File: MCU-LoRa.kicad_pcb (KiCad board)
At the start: 2 copper layers, 22.9 x 49 mm, 40 parts, among them J7 castellated_1x08_P2.54, J8 castellated_1x08_P2.54, J9 Conn_02x04_Top_Bottom, SW1 SW_Push, SW2 SW_Push, U1 RFM95W-915S2, U2 STM32F411CEU6, Y1 32.758kHz, Y2 25MHz

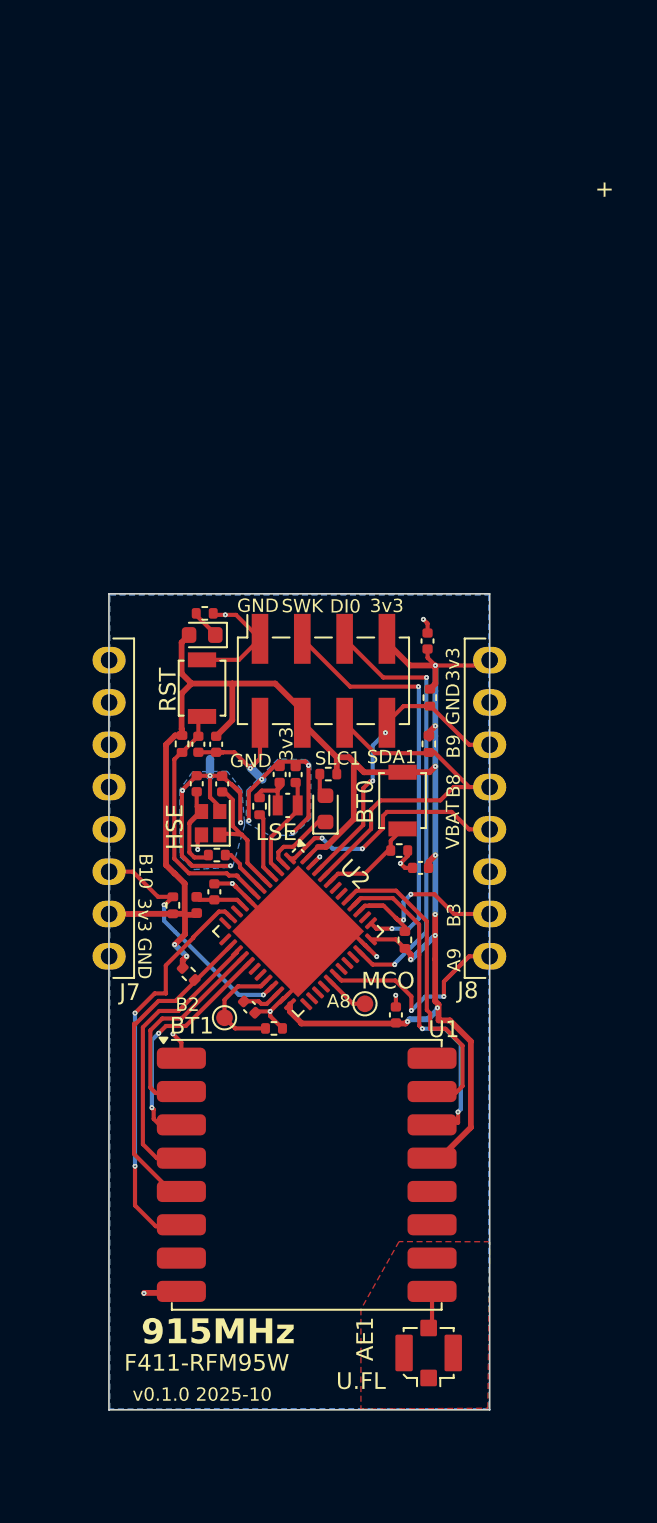
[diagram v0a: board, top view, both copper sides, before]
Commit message: reduced with of board.
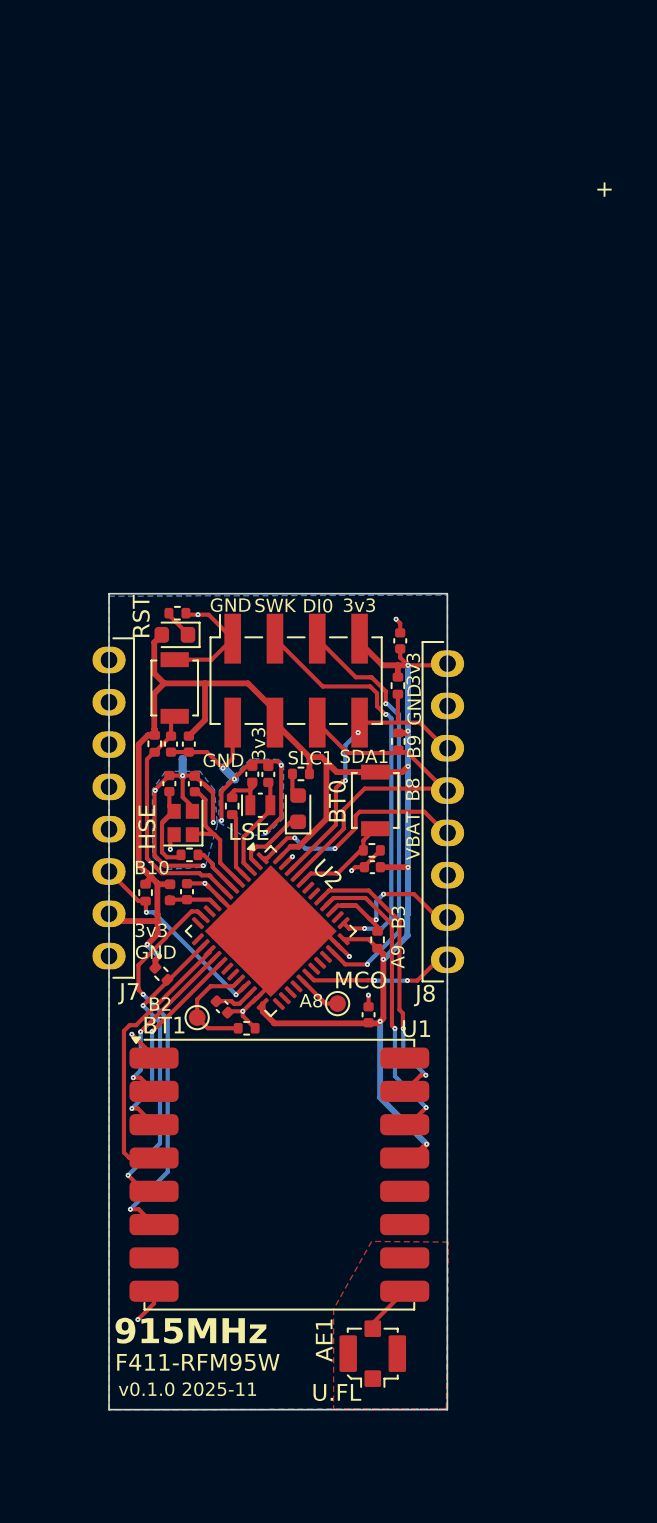
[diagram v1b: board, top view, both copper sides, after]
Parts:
- U2: footprint Package_DFN_QFN:QFN-48-1EP_7x7mm_P0.5mm_EP5.6x5.6mm -> ProjectLib:QFN-48-1EP_7x7mm_P0.5mm_EP5.6x5.6mm
- moved AE1 3.36 mm to (65.4, 91.9)
- moved C4 2.89 mm to (65.4, 62.7)
- moved J8 2.54 mm to (69.9, 59.3)
- moved R10 2.05 mm to (66.9, 51.8)
- moved R9 1.85 mm to (67.0, 55.1)
- moved R1 1.81 mm to (51.8, 64.2), turned to -90 degrees
- moved L1 1.77 mm to (53.3, 64.2), turned to 90 degrees
- moved R2 1.64 mm to (65.7, 67.0)
- moved U1 1.64 mm to (59.8, 81.1)
- moved C9 1.64 mm to (58.2, 57.1)
- moved D2 1.64 mm to (60.9, 59.2)
- moved NT1 1.64 mm to (56.8, 57.0)
- moved C7 1.64 mm to (54.3, 64.1)
- moved C1 1.64 mm to (54.4, 55.3)
- moved C10 1.64 mm to (54.7, 57.7)
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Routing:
- net +3V3: track 115.2 -> 108.7 mm, vias 11 -> 9
- net PA9: track 14.4 -> 9.61 mm
- net SCL2: track 14.6 -> 11.8 mm
- net MISO: track 12.8 -> 10.9 mm, vias 0 -> 2
- net DIO1: track 19.1 -> 17.3 mm, vias 0 -> 2
- net DIO0: track 20.5 -> 18.8 mm
- net SDA2: track 11.9 -> 10.4 mm
- net SCL1: track 21.8 -> 20.5 mm
- net VBAT: track 14.4 -> 13.3 mm
- net Net-(AE1-A): track 1.99 -> 3.04 mm
- net SCK: track 17.3 -> 16.4 mm
- net /f411/SWDIO: track 26.3 -> 25.5 mm
- net RESET: track 24.3 -> 23.6 mm
- net GND: track 34.3 -> 35.0 mm
- net /f411/SWCLK: track 25.4 -> 24.7 mm
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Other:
- board size 22.9 x 49 mm -> 20.3 x 49 mm
- board text added: "v0.1.0 2025-11"
- board text removed: "v0.1.0 2025-10"

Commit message: added QR code
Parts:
- added G***: LOGO, ProjectLib:SensorProject_QR, B.Cu at (60.0, 87.6)

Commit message: ongoing
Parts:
- removed TP1: BT1 b2, ProjectLib:TestPoint_Pad_D1.0mm
- removed TP2: MCO, ProjectLib:TestPoint_Pad_D1.0mm
- J7, J8: value castellated_1x08_P2.54 -> Conn_01x12_Pin; footprint ProjectLib:castellated_1x08_P2.54mm -> ProjectLib:Castellated_Header_1x12_P2.00mm_Vertical
- moved J9 31.5 mm to (60.4, 20.0)
- moved SW2 18.9 mm to (58.4, 70.2), turned to 180 degrees
- moved C5 14.0 mm to (59.0, 68.1), turned to 180 degrees
- moved R7 13.7 mm to (57.1, 68.1), turned to 0 degrees
- moved SW1 11.8 mm to (63.2, 70.2), turned to 180 degrees
- moved J7 10.9 mm to (49.6, 48.2), turned to 0 degrees
- moved J8 10.8 mm to (69.9, 70.2), turned to 180 degrees
- moved D2 10.6 mm to (62.9, 48.7), turned to 180 degrees
- moved R2 10.4 mm to (55.5, 68.6)
- moved C3 9.64 mm to (65.0, 61.9), turned to -135 degrees
- moved R11 8.24 mm to (60.5, 51.6), turned to 45 degrees
- moved R5 7.96 mm to (60.8, 49.1), turned to 90 degrees
- moved C9 7.54 mm to (62.7, 51.1), turned to -135 degrees
- moved R8 7.48 mm to (55.6, 65.2), turned to -135 degrees
- moved R6 7.14 mm to (61.9, 67.9)
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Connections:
- J7 pad 3: SCL2 -> unconnected-(J7-Pin_3-Pad3)
- J8 pad 1: +3V3 -> GND
- J8 pad 2: GND -> +3V3
- J8 pad 3: SDA1 -> PA8-MCO
- J8 pad 4: SCL1 -> PA9
- J8 pad 5: VBAT -> SWDIO
- J8 pad 6: unconnected-(J8-Pin_6-Pad6) -> SWCLK
- J8 pad 7: SDA2 -> unconnected-(J8-Pin_7-Pad7)
- J8 pad 8: PA9 -> SCL1
- J9 pad a1: GND -> unconnected-(J9-Pin_a1-Pada1)
- J9 pad a2: +3V3 -> unconnected-(J9-Pin_a2-Pada2)
- J9 pad a3: SCL1 -> unconnected-(J9-Pin_a3-Pada3)
- J9 pad a4: SDA1 -> unconnected-(J9-Pin_a4-Pada4)
- J9 pad b1: GND -> unconnected-(J9-Pin_b1-Padb1)
- J9 pad b2: /f411/SWCLK -> unconnected-(J9-Pin_b2-Padb2)
- J9 pad b3: /f411/SWDIO -> unconnected-(J9-Pin_b3-Padb3)
- J9 pad b4: +3V3 -> unconnected-(J9-Pin_b4-Padb4)
- U2 pad 29: Net-(U2-PA8) -> PA8-MCO
- U2 pad 34: /f411/SWDIO -> SWDIO
- U2 pad 37: /f411/SWCLK -> SWCLK
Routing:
- net /f411/SWDIO: track 25.5 -> 0.00 mm, vias 2 -> 0
- net /f411/SWCLK: track 24.7 -> 0.00 mm, vias 2 -> 0
- net SCL1: track 20.5 -> 8.34 mm
- net Net-(D2-K): track 4.33 -> 14.4 mm, vias 0 -> 4
- net Net-(U2-BOOT0): track 6.04 -> 14.7 mm, vias 0 -> 4
- net PA8-MCO: track 0.00 -> 8.31 mm
- net SDA1: track 17.2 -> 10.1 mm, vias 2 -> 0
- net SWDIO: track 0.00 -> 6.27 mm
- net DIO1: track 17.3 -> 23.4 mm
- net DIO0: track 18.8 -> 24.5 mm
- net SWCLK: track 0.00 -> 5.63 mm, vias 0 -> 2
- net SDA2: track 10.4 -> 5.37 mm, vias 2 -> 0
- net Net-(U2-PB2): track 6.81 -> 1.86 mm
- net PC15_OSC32_OUT: track 4.00 -> 8.30 mm
- net PC14_OSC32_IN: track 5.71 -> 8.81 mm
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
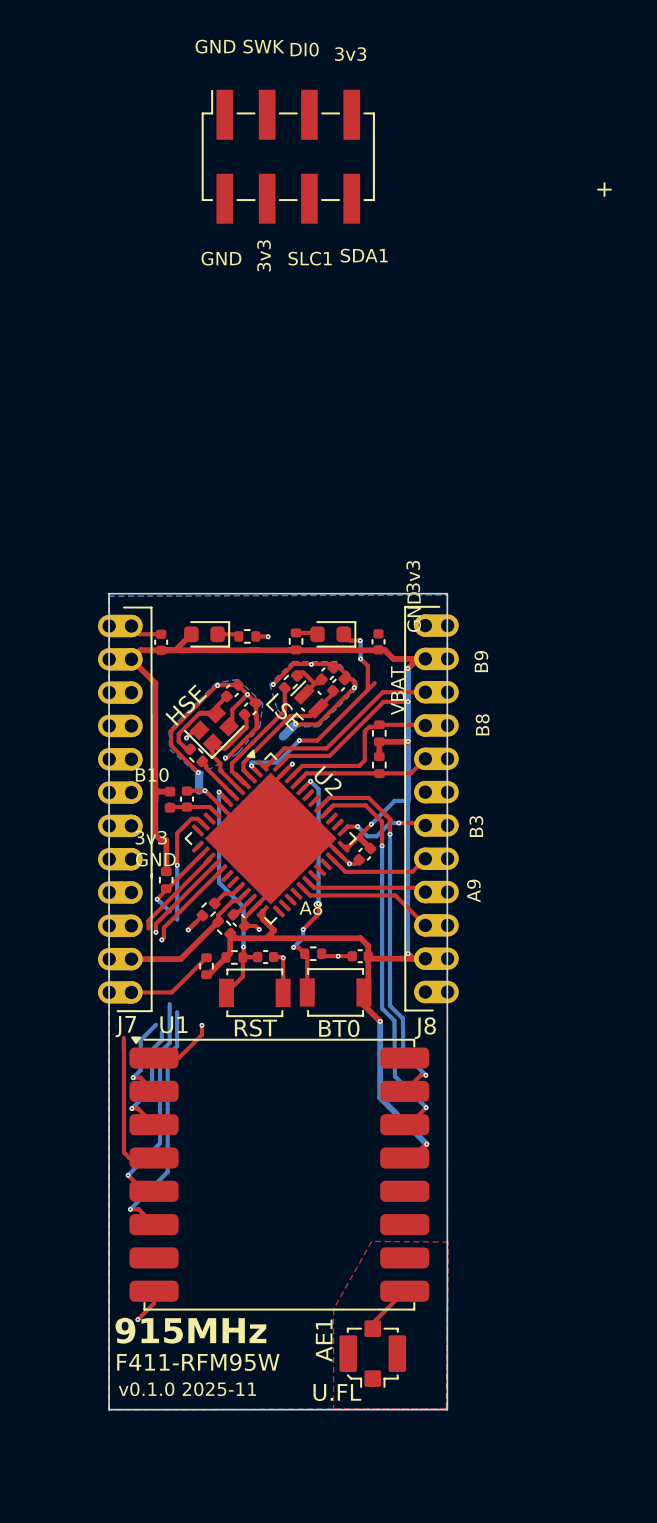
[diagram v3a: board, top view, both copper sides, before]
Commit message: settled on 24-pins. Fairly clean castillated pin header but no footprint yet. Decided against rotating radio.
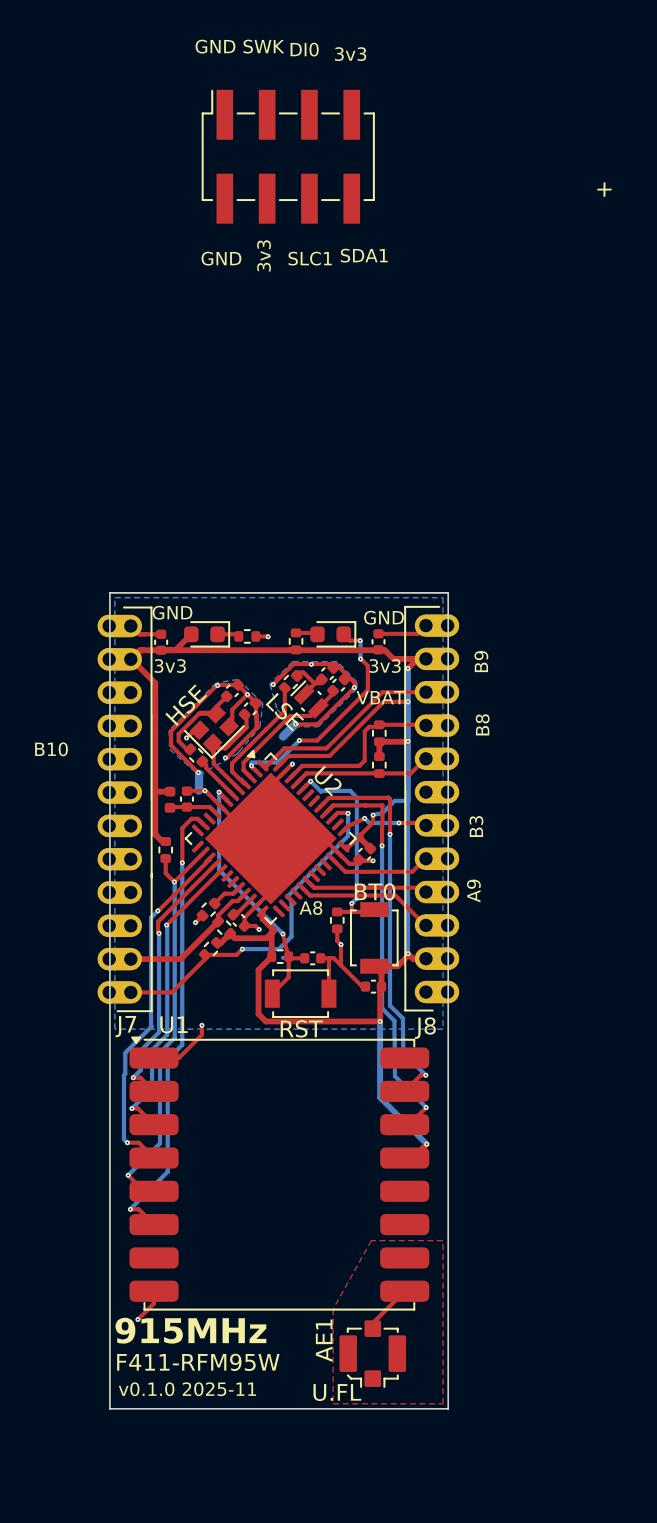
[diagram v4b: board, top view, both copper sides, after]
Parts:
- moved SW1 4.02 mm to (65.5, 66.9), turned to 90 degrees
- moved C5 2.83 mm to (61.8, 68.1)
- moved R7 2.75 mm to (59.9, 68.0)
- moved SW2 2.75 mm to (61.1, 70.3)
- moved R6 2.47 mm to (63.3, 65.9), turned to -90 degrees
- moved C4 1.99 mm to (65.5, 69.8)
- moved R3 1.81 mm to (53.0, 61.6)
- moved R2 1.07 mm to (55.7, 67.6), turned to 45 degrees
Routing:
- net SDA2: track 5.37 -> 21.3 mm, vias 0 -> 2
- net SCK: track 14.6 -> 21.3 mm, vias 0 -> 2
- net NSS: track 18.3 -> 24.3 mm
- net MISO: track 10.9 -> 16.5 mm
- net MOSI: track 12.7 -> 18.3 mm
- net RESET: track 22.1 -> 27.7 mm
- net GND: track 32.4 -> 36.1 mm, vias 10 -> 9
- net Net-(U2-BOOT0): track 14.7 -> 13.0 mm, vias 4 -> 2
- net +3V3: track 105.6 -> 106.7 mm
- net PC15_OSC32_OUT: track 8.30 -> 7.41 mm
- net Net-(U2-NRST): track 15.1 -> 15.7 mm
- net Net-(D2-K): track 14.4 -> 13.9 mm
- net SWCLK: track 5.63 -> 5.08 mm

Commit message: cleanup. ERC and DRC good. No footprint yet.
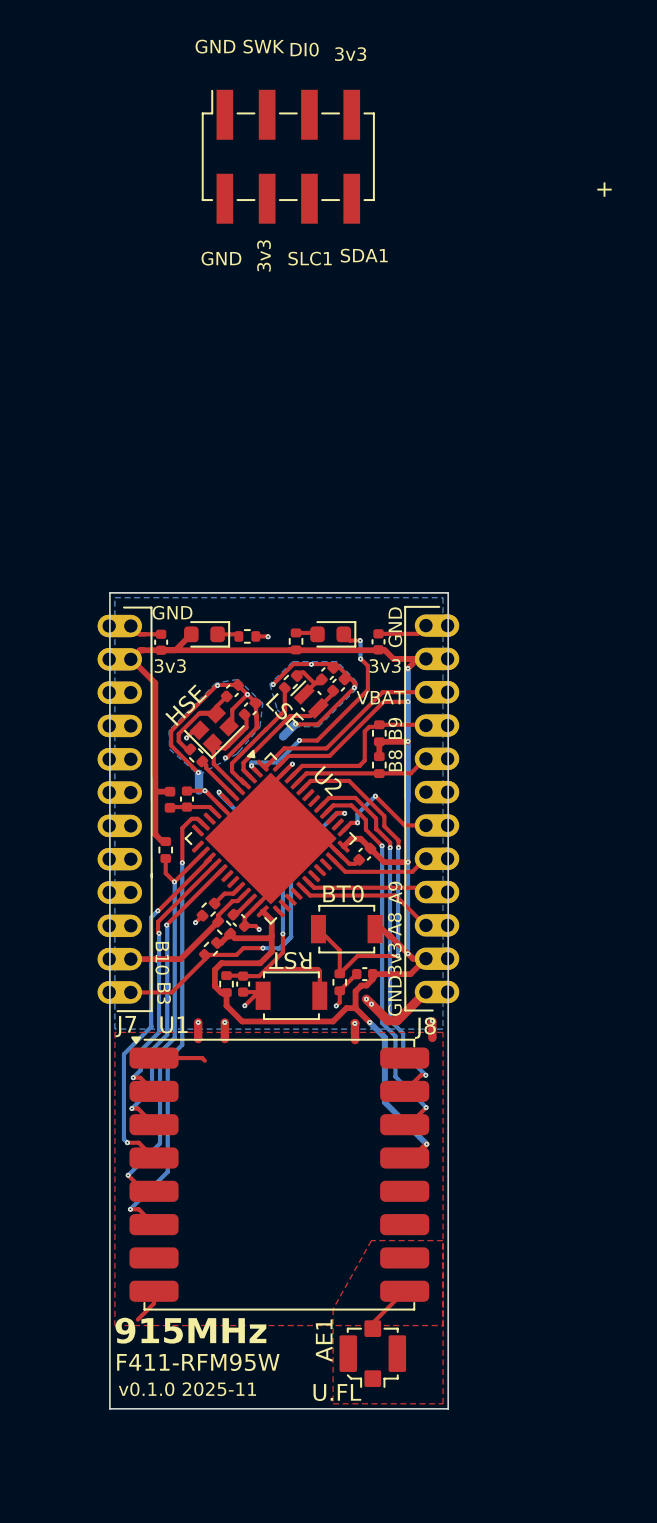
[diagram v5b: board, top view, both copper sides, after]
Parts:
- added NT3: NetTie_2, ProjectLib:NetTie-2_SMD_Pad0.5mm, F.Cu at (55.0, 72.5)
- added NT4: NetTie_2, ProjectLib:NetTie-2_SMD_Pad0.5mm, F.Cu at (56.5, 72.5)
- added NT5: NetTie_2, ProjectLib:NetTie-2_SMD_Pad0.5mm, F.Cu at (64.4, 72.5)
- added NT6: NetTie_2, ProjectLib:NetTie-2_SMD_Pad0.5mm, F.Cu at (69.0, 72.4)
- moved G*** 5.48 mm to (60.0, 82.1)
- moved C5 4.45 mm to (57.6, 69.7), turned to 90 degrees
- moved R6 3.72 mm to (63.5, 69.6)
- moved R7 3.62 mm to (56.6, 69.7), turned to 90 degrees
- moved SW1 1.74 mm to (63.9, 66.4), turned to 180 degrees
- moved C4 0.92 mm to (65.0, 69.1)
- moved SW2 0.56 mm to (60.5, 70.4), turned to 0 degrees
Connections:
- U1 pad 1: GND -> GND_RADIO
- U1 pad 8: GND -> GND_RADIO
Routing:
- net Net-(U2-BOOT0): track 13.0 -> 21.9 mm
- net +3V3: track 106.7 -> 112.8 mm
- net GND_RADIO: track 0.00 -> 5.22 mm
- net Net-(U2-NRST): track 15.7 -> 20.7 mm
- net GND: track 36.1 -> 31.2 mm, vias 9 -> 13
- net SWCLK: track 5.08 -> 6.85 mm
- net DIO1: track 23.6 -> 22.4 mm
- net DIO0: track 24.7 -> 23.7 mm
- net SDA2: track 21.3 -> 22.2 mm
- added copper zone on F.Cu, net GND_RADIO
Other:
- board text added: "PA8(MCO)"
- board text added: "SWCLK"
- board text added: "SWDIO"

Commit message: added footprint and step model. Cleaned up silkscreen and fab layers.
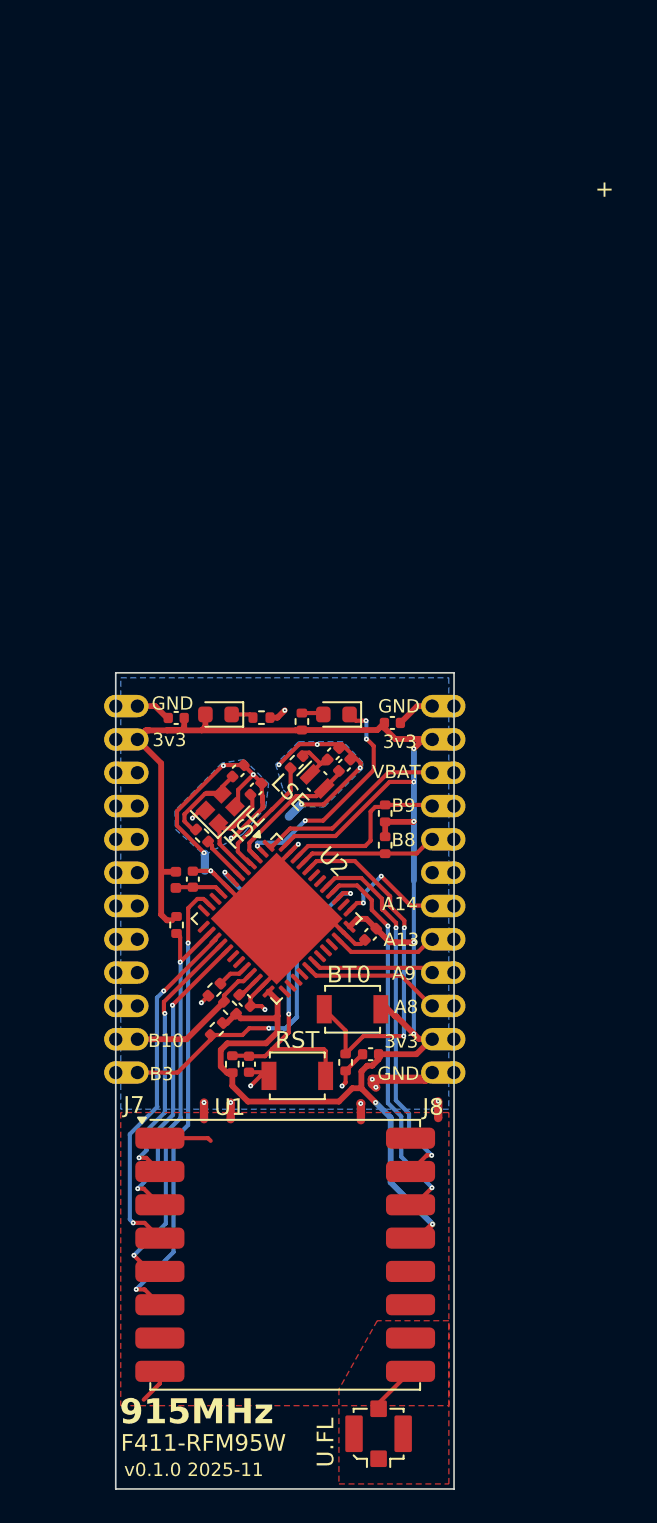
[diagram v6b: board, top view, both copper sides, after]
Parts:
- removed J9: Conn_02x04_Top_Bottom, ProjectLib:PinSocket_2x04_P2.54mm_Vertical_SMD
- moved R4 4.95 mm to (58.8, 53.7)
- moved C2 4.94 mm to (66.6, 54.0), turned to 0 degrees
- moved D1 4.88 mm to (56.2, 53.5)
- moved J8 4.85 mm to (70.3, 75.0)
- moved J7 4.83 mm to (50.0, 53.0)
- moved C10 4.82 mm to (58.4, 58.0)
- moved C11 4.82 mm to (57.4, 56.9)
- moved C5 4.82 mm to (58.0, 74.5)
- moved C6 4.82 mm to (57.8, 70.7)
- moved C9 4.82 mm to (63.1, 55.9)
- moved D2 4.82 mm to (63.2, 53.5)
- moved G*** 4.82 mm to (60.3, 86.9)
- moved NT2 4.82 mm to (55.4, 62.4)
- moved NT4 4.82 mm to (56.9, 77.3)
- moved R1 4.82 mm to (56.9, 71.1)
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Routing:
- net GND: track 31.2 -> 29.5 mm
- net +3V3: track 112.8 -> 113.9 mm
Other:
- board text added: "(SDA2)PB3"
- board text added: "A13"
- board text added: "A14"
- board text added: "PA13(SWDIO)"
- board text added: "PA14(SWCLK)"
- board text removed: "DI0"
- board text removed: "PB3(SDA2)"
- board text removed: "SDA1"
- board text removed: "SLC1"
- board text removed: "SWCLK"
- board text removed: "SWDIO"
- board text removed: "SWK"
